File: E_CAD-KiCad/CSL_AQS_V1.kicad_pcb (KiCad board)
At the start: 2 copper layers, 165.1 x 54.6 mm, 262 parts, among them J2 Grove STEMMA, J3 Grove STEMMA

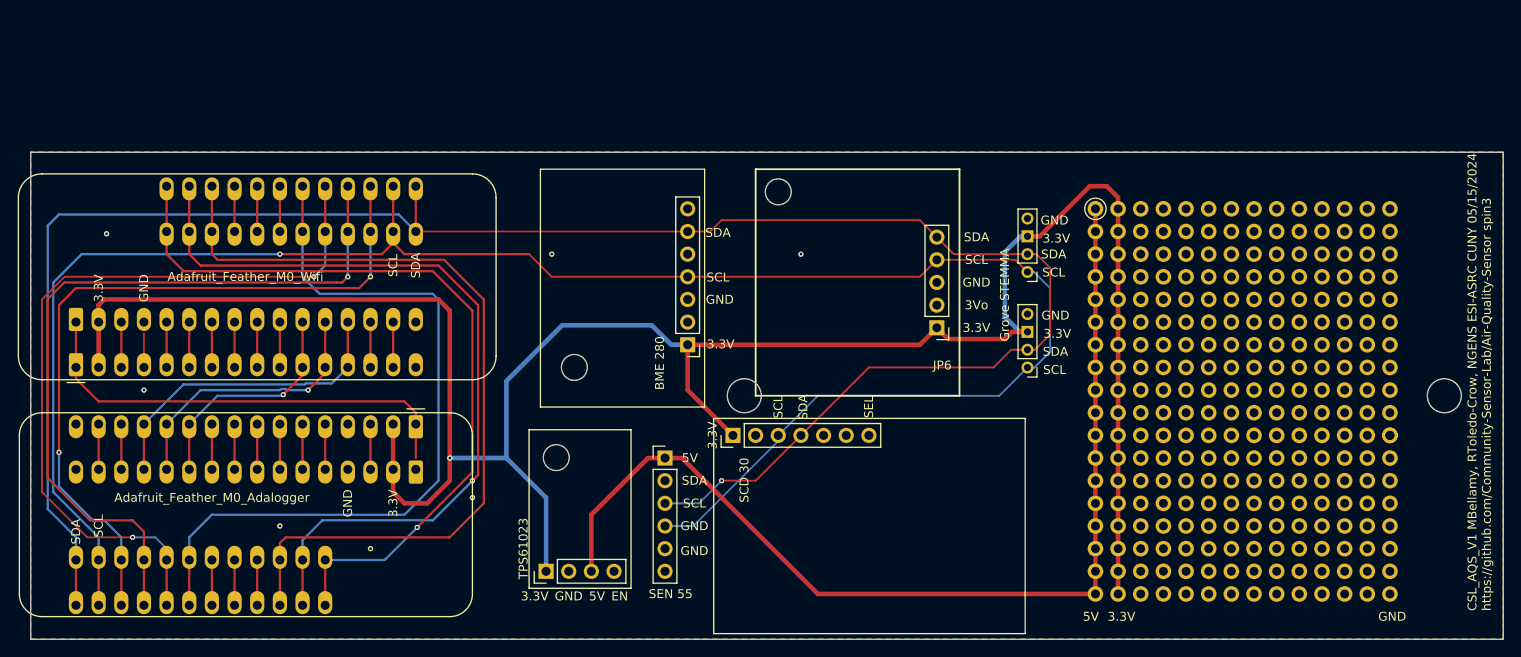
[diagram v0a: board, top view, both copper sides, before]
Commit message: Updated KiCAD Files
Fixed issue with reset pin not working when stacked on either Adafruit component. Fixed issue with improper labeling of SEN55. (Connections were correct)
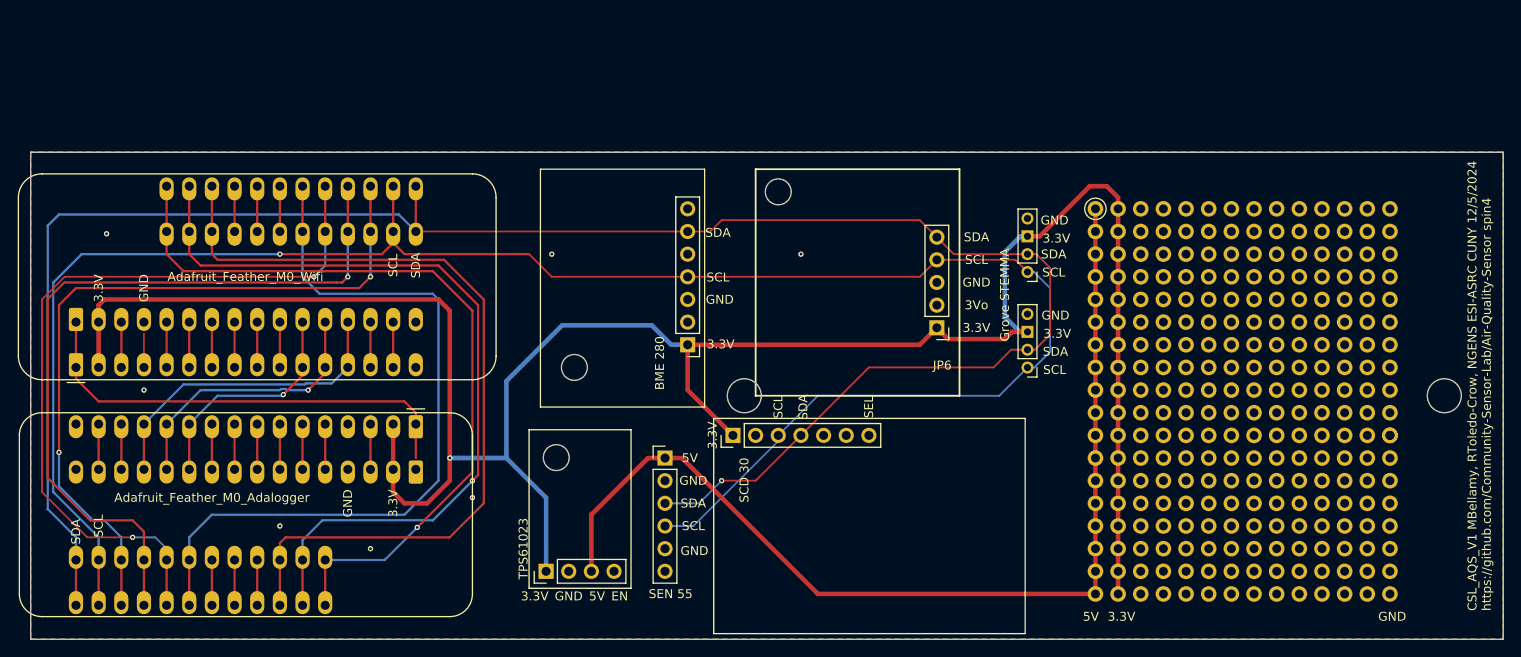
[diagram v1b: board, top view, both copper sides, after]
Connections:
- JP8 pad 2: SDA -> GND
- JP8 pad 3: SCL -> SDA
- JP8 pad 4: GND -> SCL
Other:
- board text added: "CSL_AQS_V1 MBellamy, RToledo-Crow, NGENS ESI-ASRC CUNY 12/5/2024 https://github.com/Community-Sensor-Lab/Air-Quality-Sensor spin4"
- board text removed: "CSL_AQS_V1 MBellamy, RToledo-Crow, NGENS ESI-ASRC CUNY 05/15/2024 https://github.com/Community-Sensor-Lab/Air-Quality-Sensor spin3"
